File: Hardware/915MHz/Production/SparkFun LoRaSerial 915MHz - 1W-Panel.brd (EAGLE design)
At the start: 122.2 x 153.5 mm, 846 parts, among them J1 QWIIC_RIGHT_ANGLE, J11 USB C, J12 QWIIC_RIGHT_ANGLE, J13 JTAG, J16 USB C, J17 QWIIC_RIGHT_ANGLE, J18 JTAG, J2 USB C, J21 USB C, J22 QWIIC_RIGHT_ANGLE, J23 JTAG, J26 USB C, J27 QWIIC_RIGHT_ANGLE, J28 JTAG, J3 USB C, J31 USB C, J32 QWIIC_RIGHT_ANGLE, J33 JTAG, J36 USB C, J37 QWIIC_RIGHT_ANGLE, J38 JTAG, J4 JTAG, J41 USB C, J42 QWIIC_RIGHT_ANGLE, J43 JTAG, J46 USB C, J47 QWIIC_RIGHT_ANGLE, J48 JTAG, J7 QWIIC_RIGHT_ANGLE, J8 JTAG, Q1 20V/0.2A/8MHz/1.2Ω/1Vth, Q10 20V/0.2A/8MHz/1.2Ω/1Vth, Q11 20V/0.2A/8MHz/1.2Ω/1Vth, Q12 20V/0.2A/8MHz/1.2Ω/1Vth, Q13 20V/0.2A/8MHz/1.2Ω/1Vth, Q14 20V/0.2A/8MHz/1.2Ω/1Vth, Q15 20V/0.2A/8MHz/1.2Ω/1Vth, Q16 20V/0.2A/8MHz/1.2Ω/1Vth, Q17 20V/0.2A/8MHz/1.2Ω/1Vth, Q18 20V/0.2A/8MHz/1.2Ω/1Vth, Q19 20V/0.2A/8MHz/1.2Ω/1Vth, Q2 20V/0.2A/8MHz/1.2Ω/1Vth, Q20 20V/0.2A/8MHz/1.2Ω/1Vth, Q3 20V/0.2A/8MHz/1.2Ω/1Vth, Q4 20V/0.2A/8MHz/1.2Ω/1Vth, Q5 20V/0.2A/8MHz/1.2Ω/1Vth, Q6 20V/0.2A/8MHz/1.2Ω/1Vth, Q7 20V/0.2A/8MHz/1.2Ω/1Vth, Q8 20V/0.2A/8MHz/1.2Ω/1Vth, Q9 20V/0.2A/8MHz/1.2Ω/1Vth, U1 AP2112K-3.3, U10 AP2112K-3.3, U11 E19-915M30S, U12 ATSAMD21G-A, U13 AP2112K-3.3, U14 E19-915M30S, U15 ATSAMD21G-A, U16 AP2112K-3.3, U17 E19-915M30S, U18 ATSAMD21G-A, U19 AP2112K-3.3, U2 ATSAMD21G-A, U20 E19-915M30S, U21 ATSAMD21G-A, U22 AP2112K-3.3, U23 E19-915M30S, U24 ATSAMD21G-A, U25 AP2112K-3.3, U26 E19-915M30S, U27 ATSAMD21G-A, U28 AP2112K-3.3, U29 E19-915M30S, U3 AP2112K-3.3, U30 ATSAMD21G-A, U4 E19-915M30S, U5 E19-915M30S, U6 ATSAMD21G-A, U7 AP2112K-3.3, U8 E19-915M30S, U9 ATSAMD21G-A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

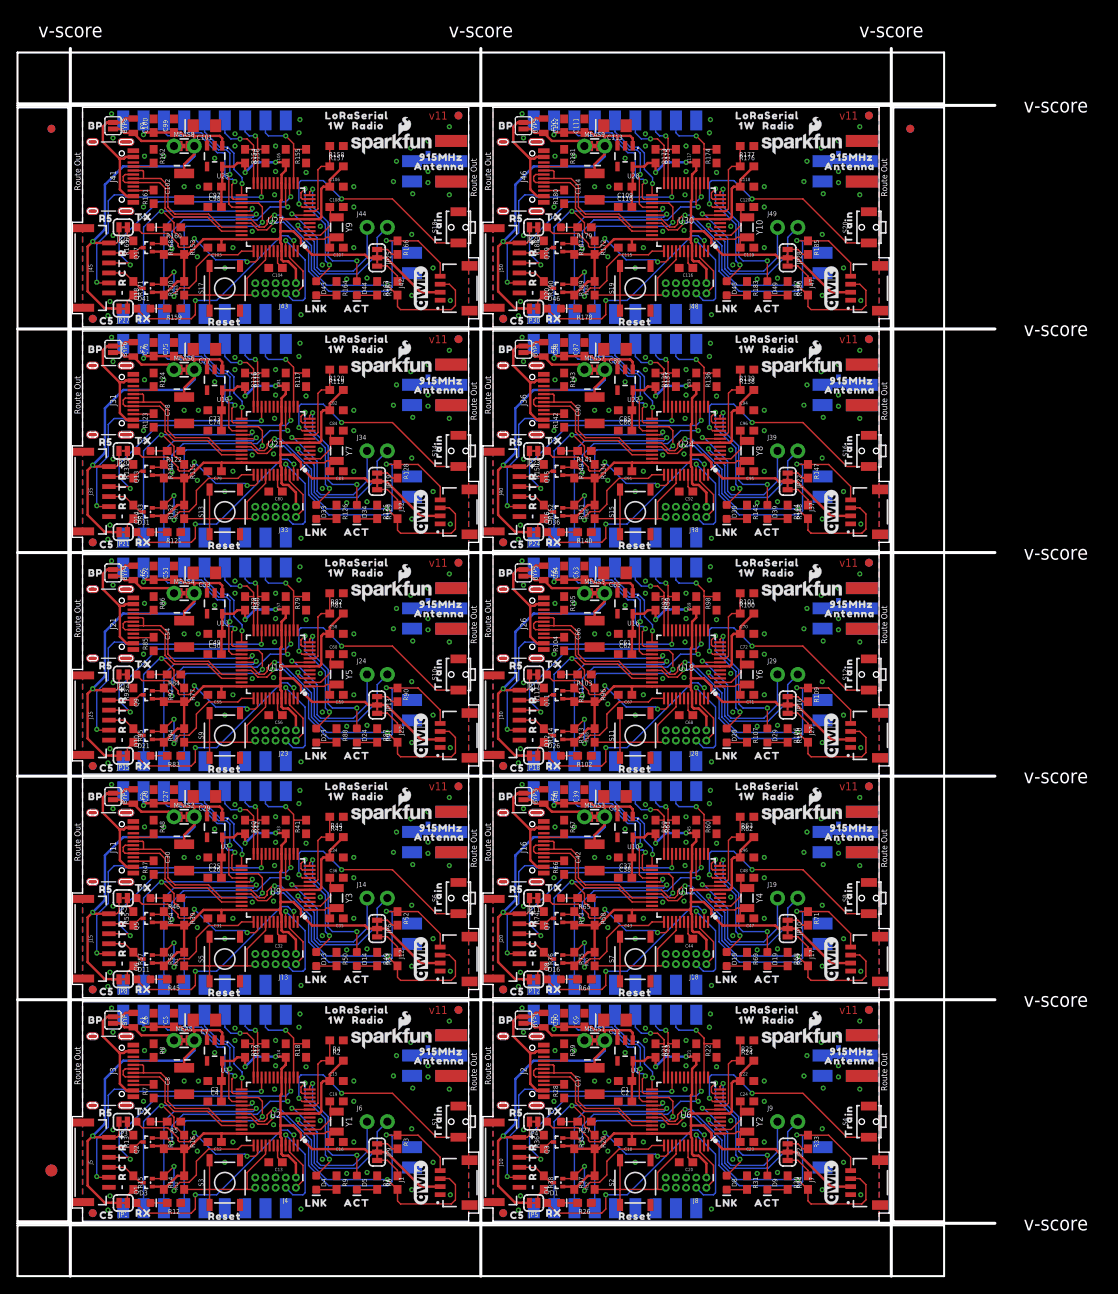
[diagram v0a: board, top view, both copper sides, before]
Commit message: Add RSSI LEDs
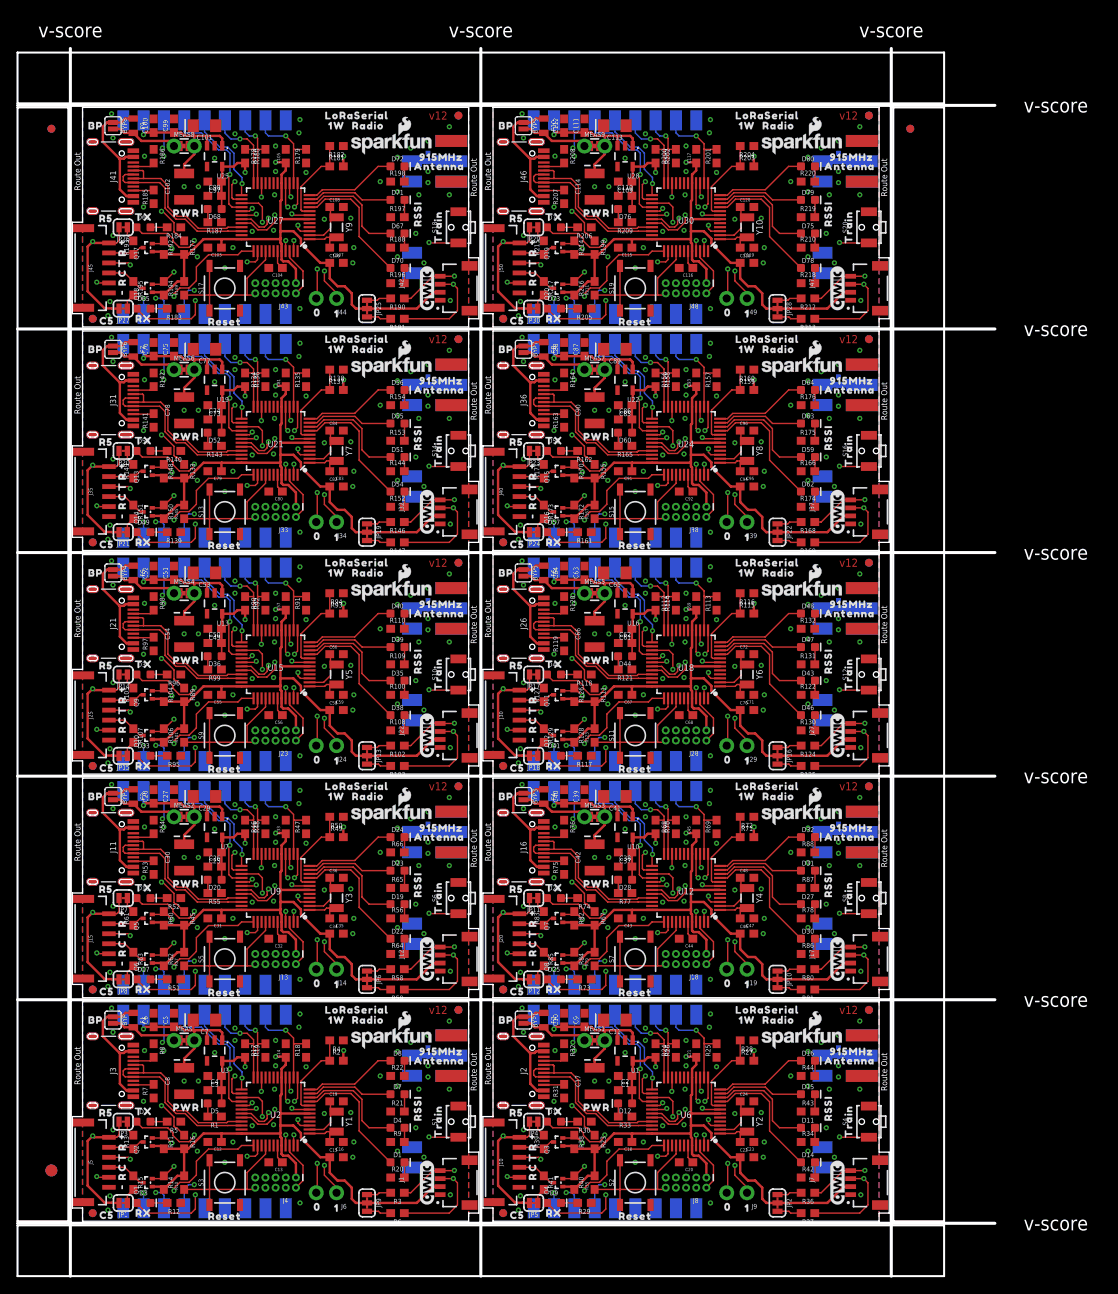
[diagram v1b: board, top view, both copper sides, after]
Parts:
- added D51, D54, D55, D56, D59, D62, D63, D64, D67, D70, D71, D72, D75, D78, D79, D80: GREEN, SparkFun-LED:LED-0603
- added D52, D60, D68, D76: RED, SparkFun-LED:LED-0603
- added D53, D61, D69, D77: PESD0402, SparkFun-DiscreteSemi:0402-TIGHT
- added D57, D65, D73: Yellow, SparkFun-LED:LED-0603
- added D58, D66, D74: BLUE, SparkFun-LED:LED-0603
- added R191, R192, R193, R194, R195, R212, R213, R214, R215, R216, R217: 2.2k, SparkFun-Resistors:0603
- added R196, R197, R198, R205, R210, R218, R219, R220: 4.7k, SparkFun-Resistors:0603
- added R199, R200, R201, R202: 100k, SparkFun-Resistors:0603
- added R203, R204, R211: 10k, SparkFun-Resistors:0603
- added R206, R209: 1k, SparkFun-Resistors:0603
- added R207, R208: 5.1k, SparkFun-Resistors:0603
- added U$201: (no value), output:ANTENNA1
- added U$202: (no value), output:RADIO2
- added U$203: (no value), output:RX1
- added U$204: (no value), output:TX0
- added U$205: (no value), output:#0
- added U$206: (no value), output:#1
- added U$207: (no value), output:R3
- added U$208: (no value), output:T2
- added U$209: (no value), output:C0
- added U$210: (no value), output:R1
- added U$211: (no value), output:LORASERIAL0
- added U$212: (no value), output:1W1
- added U$213: (no value), output:TRAIN0
- added U$214: (no value), output:BP0
- added U$215: (no value), output:C50
- added U$216: (no value), output:R50
- added U$217: (no value), output:RSSI0
- added U$218: (no value), output:PWR0
- added U$219: (no value), output:01
- added U$220: (no value), output:10
- D1, D11, D16, D31, D46: value Yellow -> GREEN
- D10, D50: value PESD0402 -> BLUE; device SparkFun-DiscreteSemi:0402-TIGHT -> SparkFun-LED:LED-0603
- D12: value GREEN -> RED
- D13: value BLUE -> PESD0402; device SparkFun-LED:LED-0603 -> SparkFun-DiscreteSemi:0402-TIGHT
- D14, D19, D24, D39: value RED -> GREEN
- D15, D30, D35, D40: value PESD0402 -> GREEN; device SparkFun-DiscreteSemi:0402-TIGHT -> SparkFun-LED:LED-0603
- D17: value GREEN -> Yellow
- D2, D42: value GREEN -> BLUE
- D20: value PESD0402 -> RED; device SparkFun-DiscreteSemi:0402-TIGHT -> SparkFun-LED:LED-0603
- D21: value Yellow -> PESD0402; device SparkFun-LED:LED-0603 -> SparkFun-DiscreteSemi:0402-TIGHT
- D23, D38, D4, D43, D48, D8: value BLUE -> GREEN
- D25: value PESD0402 -> Yellow; device SparkFun-DiscreteSemi:0402-TIGHT -> SparkFun-LED:LED-0603
- D26: value Yellow -> BLUE
- D28: value BLUE -> RED
- D29: value RED -> PESD0402; device SparkFun-LED:LED-0603 -> SparkFun-DiscreteSemi:0402-TIGHT
- D33: value BLUE -> Yellow
- D34: value RED -> BLUE
- D36: value Yellow -> RED
- D37: value GREEN -> PESD0402; device SparkFun-LED:LED-0603 -> SparkFun-DiscreteSemi:0402-TIGHT
- D49, D9: value RED -> Yellow
- R100, R108, R139, R176, R43, R44, R51: value 10k -> 4.7k
- R102, R103, R83, R84: value 4.7k -> 2.2k
- R104, R105, R124, R85: value 5.1k -> 2.2k
- R106, R107, R125, R126: value 1k -> 2.2k
- R109, R110, R130, R131, R132, R152, R166, R188, R34, R56, R73, R95: value 2.2k -> 4.7k
- R111, R112, R113, R114, R133, R90, R91, R92: value 2.2k -> 100k
- R115, R116, R137, R79: value 100k -> 10k
- R117, R153, R154, R174, R175, R20, R21, R22, R42, R78: value 100k -> 4.7k
- R118, R77, R96, R99: value 100k -> 1k
- R119, R120, R32: value 10k -> 5.1k
- R121, R140, R5: value 4.7k -> 1k
- R123, R181, R28: value 5.1k -> 10k
- R127, R146, R62, R63, R81, R82: value 10k -> 2.2k
- R141: value 4.7k -> 5.1k
- R143, R162: value 5.1k -> 1k
- R144, R183, R87, R88, R9: value 1k -> 4.7k
- R145, R182, R49, R50: value 1k -> 10k
- R157, R158, R177, R24, R25, R70, R89: value 10k -> 100k
- R159, R160, R27: value 4.7k -> 10k
- R161, R29, R66, R86: value 5.1k -> 4.7k
- R163, R164, R31: value 1k -> 5.1k
- R165, R184: value 10k -> 1k
- R167, R189, R35, R57, R71, R72, R93, R94: value 2.2k -> 10k
- R172, R173, R39, R40, R41, R58, R59, R60, R61, R80: value 100k -> 2.2k
- R178, R179, R26, R45, R46: value 4.7k -> 100k
- R180, R47, R48, R67: value 5.1k -> 100k
- R185, R186, R53, R54, R75, R76: value 2.2k -> 5.1k
- R187, R33, R52, R55, R74: value 2.2k -> 1k
- R68, R69: value 1k -> 100k
- R97, R98: value 100k -> 5.1k
- U$100: device output:R50 -> output:R1
- U$101: device output:RESET0 -> output:LORASERIAL0
- U$102: device output:915MHZ0 -> output:1W1
- U$103: device output:ANTENNA1 -> output:TRAIN0
- U$104: device output:RADIO2 -> output:BP0
- U$105: device output:ACT3 -> output:C50
- U$106: device output:LNK2 -> output:R50
- U$107: device output:RX1 -> output:RSSI0
- U$108: device output:TX0 -> output:PWR0
- U$109: device output:#0 -> output:01
- U$110: device output:#1 -> output:10
- U$111: device output:R3 -> output:RESET0
- U$112: device output:T2 -> output:915MHZ0
- U$113: device output:C0 -> output:ANTENNA1
- U$114: device output:R1 -> output:RADIO2
- U$115: device output:LORASERIAL0 -> output:RX1
- U$116: device output:1W1 -> output:TX0
- U$117: device output:TRAIN0 -> output:#0
- U$118: device output:BP0 -> output:#1
- U$119: device output:C50 -> output:R3
- U$120: device output:R50 -> output:T2
- U$121: device output:RESET0 -> output:C0
- U$122: device output:915MHZ0 -> output:R1
- U$123: device output:ANTENNA1 -> output:LORASERIAL0
- U$124: device output:RADIO2 -> output:1W1
- U$125: device output:ACT3 -> output:TRAIN0
- U$126: device output:LNK2 -> output:BP0
- U$127: device output:RX1 -> output:C50
- U$128: device output:TX0 -> output:R50
- U$129: device output:#0 -> output:RSSI0
- U$130: device output:#1 -> output:PWR0
- U$131: device output:R3 -> output:01
- U$132: device output:T2 -> output:10
- U$133: device output:C0 -> output:RESET0
- U$134: device output:R1 -> output:915MHZ0
- U$135: device output:LORASERIAL0 -> output:ANTENNA1
- U$136: device output:1W1 -> output:RADIO2
- U$137: device output:TRAIN0 -> output:RX1
- U$138: device output:BP0 -> output:TX0
- U$139: device output:C50 -> output:#0
- U$140: device output:R50 -> output:#1
- U$141: device output:RESET0 -> output:R3
- U$142: device output:915MHZ0 -> output:T2
- U$143: device output:ANTENNA1 -> output:C0
- U$144: device output:RADIO2 -> output:R1
- U$145: device output:ACT3 -> output:LORASERIAL0
- U$146: device output:LNK2 -> output:1W1
- U$147: device output:RX1 -> output:TRAIN0
- U$148: device output:TX0 -> output:BP0
- U$149: device output:#0 -> output:C50
- U$150: device output:#1 -> output:R50
- U$151: device output:R3 -> output:RSSI0
- U$152: device output:T2 -> output:PWR0
- U$153: device output:C0 -> output:01
- U$154: device output:R1 -> output:10
- U$155: device output:LORASERIAL0 -> output:RESET0
- U$156: device output:1W1 -> output:915MHZ0
- U$157: device output:TRAIN0 -> output:ANTENNA1
- U$158: device output:BP0 -> output:RADIO2
- U$159: device output:C50 -> output:RX1
- U$160: device output:R50 -> output:TX0
- U$161: device output:RESET0 -> output:#0
- U$162: device output:915MHZ0 -> output:#1
- U$163: device output:ANTENNA1 -> output:R3
- U$164: device output:RADIO2 -> output:T2
- U$165: device output:ACT3 -> output:C0
- U$166: device output:LNK2 -> output:R1
- U$167: device output:RX1 -> output:LORASERIAL0
- U$168: device output:TX0 -> output:1W1
- U$169: device output:#0 -> output:TRAIN0
- U$170: device output:#1 -> output:BP0
- U$171: device output:R3 -> output:C50
- U$172: device output:T2 -> output:R50
- U$173: device output:C0 -> output:RSSI0
- U$174: device output:R1 -> output:PWR0
- U$175: device output:LORASERIAL0 -> output:01
- U$176: device output:1W1 -> output:10
- U$177: device output:TRAIN0 -> output:RESET0
- U$178: device output:BP0 -> output:915MHZ0
- U$179: device output:C50 -> output:ANTENNA1
- U$180: device output:R50 -> output:RADIO2
- U$181: device output:RESET0 -> output:RX1
- U$182: device output:915MHZ0 -> output:TX0
- U$183: device output:ANTENNA1 -> output:#0
- U$184: device output:RADIO2 -> output:#1
- U$185: device output:ACT3 -> output:R3
- U$186: device output:LNK2 -> output:T2
- U$187: device output:RX1 -> output:C0
- U$188: device output:TX0 -> output:R1
- U$189: device output:#0 -> output:LORASERIAL0
- U$190: device output:#1 -> output:1W1
- U$191: device output:R3 -> output:TRAIN0
- U$192: device output:T2 -> output:BP0
- U$193: device output:C0 -> output:C50
- U$194: device output:R1 -> output:R50
- U$195: device output:LORASERIAL0 -> output:RSSI0
- U$196: device output:1W1 -> output:PWR0
- U$197: device output:TRAIN0 -> output:01
- U$198: device output:BP0 -> output:10
- U$199: device output:C50 -> output:RESET0
- U$200: device output:R50 -> output:915MHZ0
- U$21, U$41: device output:RESET0 -> output:RSSI0
- U$22: device output:915MHZ0 -> output:10
- U$23: device output:ANTENNA1 -> output:RESET0
- U$24: device output:RADIO2 -> output:915MHZ0
- U$25: device output:ACT3 -> output:ANTENNA1
- U$26: device output:LNK2 -> output:RADIO2
- U$42: device output:915MHZ0 -> output:PWR0
- U$43: device output:ANTENNA1 -> output:01
- U$44: device output:RADIO2 -> output:10
- U$45: device output:ACT3 -> output:RESET0
- U$46: device output:LNK2 -> output:915MHZ0
- U$47: device output:RX1 -> output:ANTENNA1
- U$48: device output:TX0 -> output:RADIO2
- U$49: device output:#0 -> output:RX1
- U$50: device output:#1 -> output:TX0
- U$51: device output:R3 -> output:#0
- U$52: device output:T2 -> output:#1
- U$53: device output:C0 -> output:R3
- U$54: device output:R1 -> output:T2
- U$55: device output:LORASERIAL0 -> output:C0
- U$56: device output:1W1 -> output:R1
- U$57: device output:TRAIN0 -> output:LORASERIAL0
- U$58: device output:BP0 -> output:1W1
- U$59: device output:C50 -> output:TRAIN0
- U$6, U$65: device output:ACT3 -> output:01
- U$60: device output:R50 -> output:BP0
- U$61: device output:RESET0 -> output:C50
- U$62: device output:915MHZ0 -> output:R50
- U$63: device output:ANTENNA1 -> output:RSSI0
- U$64: device output:RADIO2 -> output:PWR0
- U$66: device output:LNK2 -> output:10
- U$67: device output:RX1 -> output:RESET0
- U$68: device output:TX0 -> output:915MHZ0
- U$69: device output:#0 -> output:ANTENNA1
- U$7, U$86: device output:LNK2 -> output:PWR0
- U$70: device output:#1 -> output:RADIO2
- U$71: device output:R3 -> output:RX1
- U$72: device output:T2 -> output:TX0
- U$73: device output:C0 -> output:#0
- U$74: device output:R1 -> output:#1
- U$75: device output:LORASERIAL0 -> output:R3
- U$76: device output:1W1 -> output:T2
- U$77: device output:TRAIN0 -> output:C0
- U$78: device output:BP0 -> output:R1
- U$79: device output:C50 -> output:LORASERIAL0
- U$80: device output:R50 -> output:1W1
- U$81: device output:RESET0 -> output:TRAIN0
- U$82: device output:915MHZ0 -> output:BP0
- U$83: device output:ANTENNA1 -> output:C50
- U$84: device output:RADIO2 -> output:R50
- U$85: device output:ACT3 -> output:RSSI0
- U$87: device output:RX1 -> output:01
- U$88: device output:TX0 -> output:10
- U$89: device output:#0 -> output:RESET0
- U$90: device output:#1 -> output:915MHZ0
- U$91: device output:R3 -> output:ANTENNA1
- U$92: device output:T2 -> output:RADIO2
- U$93: device output:C0 -> output:RX1
- U$94: device output:R1 -> output:TX0
- U$95: device output:LORASERIAL0 -> output:#0
- U$96: device output:1W1 -> output:#1
- U$97: device output:TRAIN0 -> output:R3
- U$98: device output:BP0 -> output:T2
- U$99: device output:C50 -> output:C0
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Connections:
- removed net A20: U21.10
- removed net A21: J39.1, U24.7
- removed net A22: J39.2, U24.3
- removed net A23: U24.10
- removed net A24: J44.1, U27.7
- removed net A25: J44.2, U27.3
- removed net A26: U27.10
- removed net A27: J49.1, U30.7
- removed net A28: J49.2, U30.3
- removed net A29: U30.10
- removed net A3/TRAIN: S1.1, U2.9
- removed net A3/TRAIN1: S4.1, U6.9
- removed net A3/TRAIN2: S6.1, U9.9
- removed net A3/TRAIN3: S8.1, U12.9
- removed net A3/TRAIN4: S10.1, U15.9
- removed net A3/TRAIN5: S12.1, U18.9
- removed net A3/TRAIN6: S14.1, U21.9
- removed net A3/TRAIN7: S16.1, U24.9
- removed net A3/TRAIN8: S18.1, U27.9
- removed net A3/TRAIN9: S20.1, U30.9
- removed net D31: U24.19
- removed net D32: U24.20
- removed net D33: U27.13
- removed net D34: U27.21
- removed net D35: U27.19
- removed net D36: U27.20
- removed net D37: U30.13
- removed net D38: U30.21
- removed net D39: U30.19
- removed net D40: U30.20
- removed net D8/LINK: D4.A, U2.11
- removed net D8/LINK1: D8.A, U6.11
- removed net D8/LINK2: D13.A, U9.11
- removed net D8/LINK3: D18.A, U12.11
- removed net D8/LINK4: D23.A, U15.11
- removed net D8/LINK5: D28.A, U18.11
- removed net D8/LINK6: D33.A, U21.11
- removed net D8/LINK7: D38.A, U24.11
- removed net D8/LINK8: D43.A, U27.11
- removed net D8/LINK9: D48.A, U30.11
- removed net D9/ACT: D5.A, U2.12
- removed net D9/ACT1: D9.A, U6.12
- removed net D9/ACT2: D14.A, U9.12
- removed net D9/ACT3: D19.A, U12.12
- removed net D9/ACT4: D24.A, U15.12
- removed net D9/ACT5: D29.A, U18.12
- removed net D9/ACT6: D34.A, U21.12
- removed net D9/ACT7: D39.A, U24.12
- removed net D9/ACT8: D44.A, U27.12
- removed net D9/ACT9: D49.A, U30.12
- removed net N$14 (its old number): D7.C, R27.2
- removed net N$15 (its old number): JP4.1, R36.2
- removed net N$25 (its old number): D19.C, R68.2
- removed net N$26 (its old number): D18.C, R69.2
- removed net N$37 (its old number): D21.C, R83.2
- removed net N$47 (its old number): JP17.1, R112.2
- removed net N$48 (its old number): JP18.1, R114.2
- removed net N$58 (its old number): D38.C, R145.2
- removed net N$69 (its old number): D41.C, R159.2
- removed net N$70 (its old number): D42.C, R160.2
- removed net N$80 (its old number): JP30.1, R190.2
- new net A3/RSSI1: D1.A, U2.9
- new net A3/RSSI10: D78.A, U30.9
- new net A3/RSSI2: D14.A, U6.9
- new net A3/RSSI3: D22.A, U9.9
- new net A3/RSSI4: D30.A, U12.9
- new net A3/RSSI5: D38.A, U15.9
- new net A3/RSSI6: D46.A, U18.9
- new net A3/RSSI7: D54.A, U21.9
- new net A3/RSSI8: D62.A, U24.9
- new net A3/RSSI9: D70.A, U27.9
- new net A4/RSSI1: D11.A, U6.10
- new net A4/RSSI10: D75.A, U30.10
- new net A4/RSSI2: D4.A, U2.10
- new net A4/RSSI3: D19.A, U9.10
- new net A4/RSSI4: D27.A, U12.10
- new net A4/RSSI5: D35.A, U15.10
- new net A4/RSSI6: D43.A, U18.10
- new net A4/RSSI7: D51.A, U21.10
- new net A4/RSSI8: D59.A, U24.10
- new net A4/RSSI9: D67.A, U27.10
- new net D4/TRAIN: S1.1, U2.13
- new net D4/TRAIN1: S4.1, U6.13
- new net D4/TRAIN2: S6.1, U9.13
- new net D4/TRAIN3: S8.1, U12.13
- new net D4/TRAIN4: S10.1, U15.13
- new net D4/TRAIN5: S12.1, U18.13
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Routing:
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- added copper zone on layer 15, net GND
- added copper zone on layer 2, net GND
- added copper zone on layer 15, net GND1
- added copper zone on layer 2, net GND1
- added copper zone on layer 15, net GND2
- added copper zone on layer 2, net GND2
- added copper zone on layer 15, net GND3
- added copper zone on layer 2, net GND3
- added copper zone on layer 15, net GND4
- added copper zone on layer 2, net GND4
- added copper zone on layer 15, net GND5
- added copper zone on layer 2, net GND5
- added copper zone on layer 15, net GND6
- added copper zone on layer 2, net GND6
- added copper zone on layer 15, net GND7
- added copper zone on layer 2, net GND7
- added copper zone on layer 15, net GND8
- added copper zone on layer 2, net GND8
- added copper zone on layer 15, net GND9
- added copper zone on layer 2, net GND9
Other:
- board text added: "v12"
- board text removed: "v11"

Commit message: Adjust 50ohm microstrip for four layer
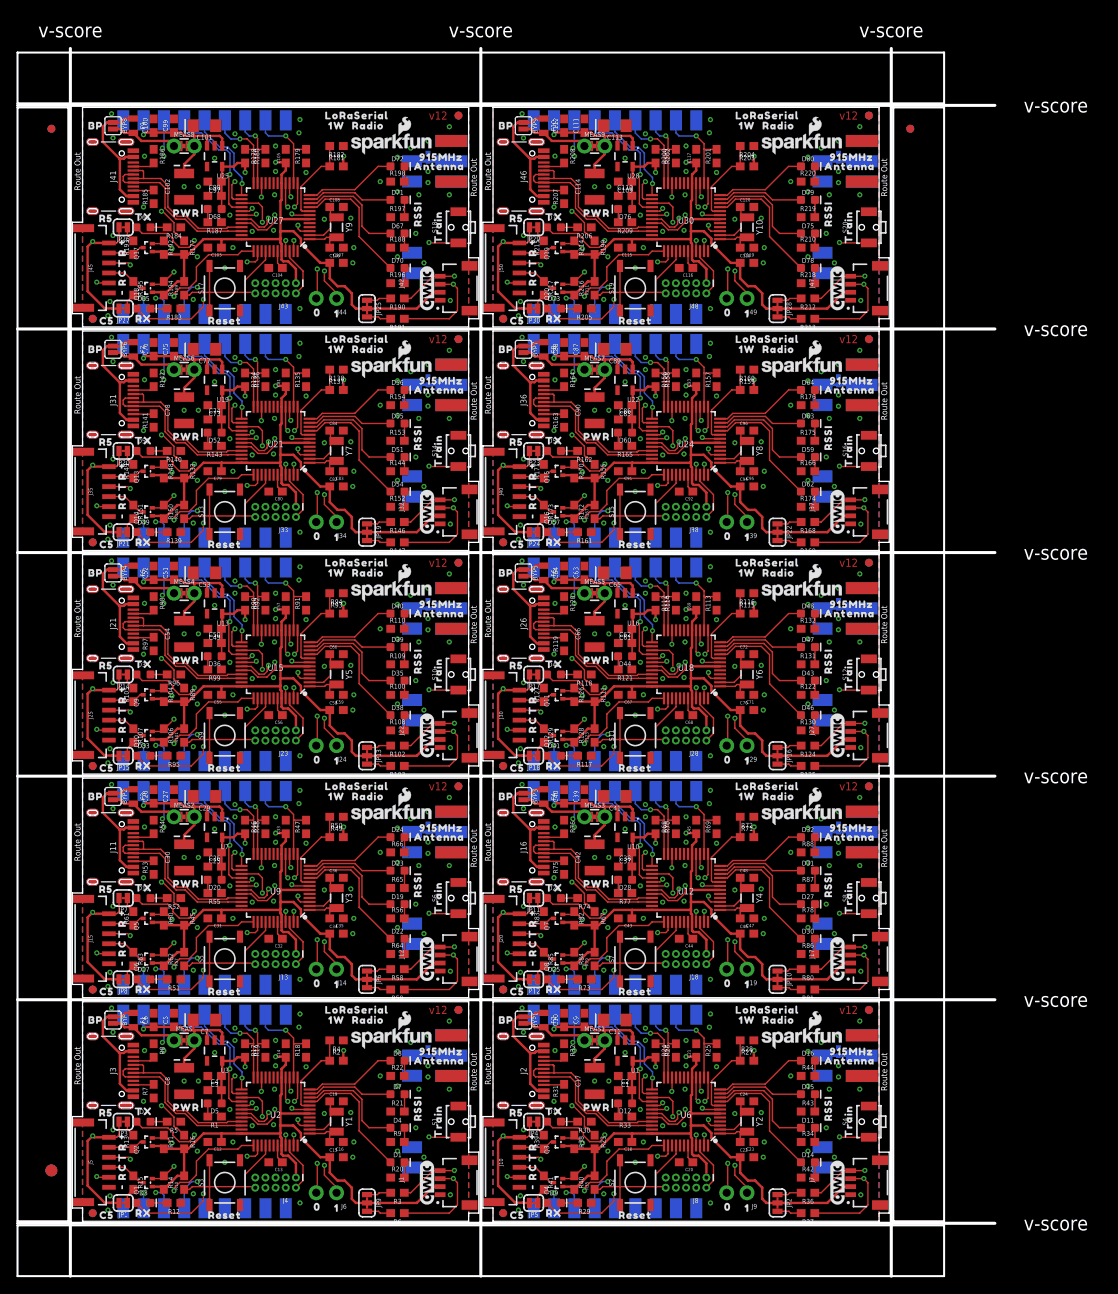
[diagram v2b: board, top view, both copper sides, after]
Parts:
- moved U$177 0.13 mm to (19.1, 112.6)
- moved U$199 0.13 mm to (70.4, 112.6)
- moved U$111 0.13 mm to (70.4, 56.7)
- moved U$89 0.13 mm to (19.1, 56.7)
- moved U$2 0.13 mm to (19.1, 0.77)
- moved U$23 0.13 mm to (70.4, 0.77)
- moved U$45 0.13 mm to (19.1, 28.7)
- moved U$67 0.13 mm to (70.4, 28.7)
- moved U$133 0.13 mm to (19.1, 84.6)
- moved U$155 0.13 mm to (70.4, 84.6)
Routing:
- net D10/LORA_D9: track 25.8 -> 26.6 mm
- net D10/LORA_D8: track 25.8 -> 26.6 mm
- net D10/LORA_D7: track 25.8 -> 26.6 mm
- net D10/LORA_D6: track 25.8 -> 26.6 mm
- net D10/LORA_D5: track 25.8 -> 26.6 mm
- net D10/LORA_D3: track 25.8 -> 26.6 mm
- net D10/LORA_D2: track 25.8 -> 26.6 mm
- net D10/LORA_D1: track 25.8 -> 26.6 mm
- net D10/LORA_D4: track 25.8 -> 26.6 mm
- net D10/LORA_D10: track 25.8 -> 26.6 mm
- net A5/RX_LED9: track 27.1 -> 26.6 mm
- net A5/RX_LED7: track 27.1 -> 26.6 mm
- net A5/RX_LED5: track 27.1 -> 26.6 mm
- net A5/RX_LED3: track 27.1 -> 26.6 mm
- net A5/RX_LED1: track 27.1 -> 26.6 mm
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
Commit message: v13 - panel files.
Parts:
- removed BYP, BYP1, BYP2, BYP3, BYP4, BYP5, BYP6, BYP7, BYP8, BYP9: JUMPER-SMT_2_NO_SILK, SparkFun-Jumpers:SMT-JUMPER_2_NO_SILK
- removed C111: 0.22uF, SparkFun-Capacitors:0603
- removed C112, C115, C116, C117, C118: 0.1uF, SparkFun-Capacitors:0603
- removed C113: 10uF, SparkFun-Capacitors:EIA3216
- removed C114: 47uF, SparkFun-Capacitors:EIA3528
- removed C119, C120: 15pF, SparkFun-Capacitors:0603
- removed MEAS, MEAS1, MEAS2, MEAS3, MEAS4, MEAS5, MEAS6, MEAS7, MEAS8, MEAS9: JUMPER-COMBO_2_NC_TRACE, SparkFun-Jumpers:COMBO-JUMPER_2_NC_TRACE
- added D81, D90: 3A/10V/280mV, SparkFun-DiscreteSemi:SOD-323
- added D82: Yellow, SparkFun-LED:LED-0603
- added D83: BLUE, SparkFun-LED:LED-0603
- added D84, D87, D88, D89: GREEN, SparkFun-LED:LED-0603
- added D85: RED, SparkFun-LED:LED-0603
- added D86: PESD0402, SparkFun-DiscreteSemi:0402-TIGHT
- added JP31, JP34, JP35, JP38, JP39: JUMPER-SMT_2_NC_TRACE_SILK, SparkFun-Jumpers:SMT-JUMPER_2_NC_TRACE_SILK
- added JP32, JP36, JP40: (no value), SparkFun-Jumpers:SMT-JUMPER_2_NC_TRACE_SILK
- added JP33, JP37: JUMPER-SMT_3_2-NC_TRACE_SILK, SparkFun-Jumpers:SMT-JUMPER_3_2-NC_TRACE_SILK
- added Q21, Q22, Q27, Q28, Q29, Q30, Q35, Q36, Q37, Q38, Q43, Q44, Q45, Q46, Q51, Q52, Q53, Q54, Q59, Q60, Q61, Q62, Q67, Q68, Q69, Q70, Q75, Q76, Q77, Q78: 600mA/40V, SparkFun-DiscreteSemi:SOT23-3
- added Q23, Q31, Q39, Q47, Q55, Q63, Q71, Q79: (no value), SparkFun-DiscreteSemi:SOT363_PHILIPS
- added Q24, Q32, Q40, Q48, Q56, Q64, Q72, Q80: 20V/4.2A/52mΩ/1.4W, SparkFun-DiscreteSemi:SOT23-3
- added Q25, Q26, Q33, Q34, Q41, Q42, Q49, Q50, Q57, Q58, Q65, Q66, Q73, Q74: 20V/0.2A/8MHz/1.2Ω/1Vth, SparkFun-DiscreteSemi:SOT-416FL
- added R221, R222, R235, R247, R248, R249, R250, R263, R275, R276, R277, R278: 1k, SparkFun-Resistors:0603
- added R223, R225, R226, R227, R228, R251, R253, R254, R255, R256, R279: 100k, SparkFun-Resistors:0603
- added R224, R252, R280: 1M, SparkFun-Resistors:0603
- added R229, R230, R237, R257, R258, R265: 10k, SparkFun-Resistors:0603
- added R231, R259: 330, SparkFun-Resistors:0603
- added R232, R260: 0, SparkFun-Resistors:0603
- added R233, R234, R261, R262: 5.1k, SparkFun-Resistors:0603
- added R236, R244, R245, R246, R264, R272, R273, R274: 220, SparkFun-Resistors:0603
- added R238, R239, R240, R241, R242, R243, R266, R267, R268, R269, R270, R271: 2.2k, SparkFun-Resistors:0603
- added TP1, TP10, TP100, TP101, TP102, TP103, TP104, TP105, TP106, TP107, TP108, TP109, TP11, TP110, TP111, TP112, TP113, TP114, TP115, TP116, TP117, TP118, TP119, TP12, TP120, TP121, TP122, TP123, TP124, TP125, TP126, TP127, TP128, TP129, TP13, TP130, TP14, TP15, TP16, TP17, TP18, TP19, TP2, TP20, TP21, TP22, TP23, TP24, TP25, TP26, TP27, TP28, TP29, TP3, TP30, TP31, TP32, TP33, TP34, TP35, TP36, TP37, TP38, TP39, TP4, TP40, TP41, TP42, TP43, TP44, TP45, TP46, TP47, TP48, TP49, TP5, TP50, TP51, TP52, TP53, TP54, TP55, TP56, TP57, TP58, TP59, TP6, TP60, TP61, TP62, TP63, TP64, TP65, TP66, TP67, TP68, TP69, TP7, TP70, TP71, TP72, TP73, TP74, TP75, TP76, TP77, TP78, TP79, TP8, TP80, TP81, TP82, TP83, TP84, TP85, TP86, TP87, TP88, TP89, TP9, TP90, TP91, TP92, TP93, TP94, TP95, TP96, TP97, TP98, TP99: (no value), SparkFun-Connectors:PAD.03X.05
- C10, C104, C38, C82, C93: value 0.1uF -> 47uF; device SparkFun-Capacitors:0603 -> SparkFun-Capacitors:EIA3528
- C100, C34, C45, C56, C58, C6, C67, C69, C80, C91: value 0.1uF -> 1.0uF
- C101, C11, C29, C41, C53: value 10uF -> 0.1uF; device SparkFun-Capacitors:EIA3216 -> SparkFun-Capacitors:0603
- C102, C78: value 47uF -> 1.0uF; device SparkFun-Capacitors:EIA3528 -> SparkFun-Capacitors:0603
- C103, C26, C70, C81, C92: value 0.1uF -> 10uF; device SparkFun-Capacitors:0603 -> SparkFun-Capacitors:EIA3216
- C107, C108, C24, C35, C72, C83, C84, C95, C96: value 15pF -> 0.1uF
- C109: value 1.0uF -> 15pF
- C110, C21, C22, C32, C33, C43, C44, C55, C76, C88, C98: value 0.1uF -> 15pF
- C17, C30, C42, C90: value 47uF -> 0.1uF; device SparkFun-Capacitors:EIA3528 -> SparkFun-Capacitors:0603
- C23, C36, C47: value 15pF -> 1.0uF
- C27: value 0.22uF -> 47uF; device SparkFun-Capacitors:0603 -> SparkFun-Capacitors:EIA3528
- C37: value 1.0uF -> 10uF; device SparkFun-Capacitors:0603 -> SparkFun-Capacitors:EIA3216
- C39, C51, C63, C75: value 0.22uF -> 0.1uF
- C48, C59: value 15pF -> 10uF; device SparkFun-Capacitors:0603 -> SparkFun-Capacitors:EIA3216
- C49: value 1.0uF -> 47uF; device SparkFun-Capacitors:0603 -> SparkFun-Capacitors:EIA3528
- C5: value 0.22uF -> 1.0uF
- C54, C66: value 47uF -> 15pF; device SparkFun-Capacitors:EIA3528 -> SparkFun-Capacitors:0603
- C60, C71: value 15pF -> 47uF; device SparkFun-Capacitors:0603 -> SparkFun-Capacitors:EIA3528
- C61, C73, C85, C97: value 1.0uF -> 0.1uF
- C65, C77: value 10uF -> 15pF; device SparkFun-Capacitors:EIA3216 -> SparkFun-Capacitors:0603
- C87, C99: value 0.22uF -> 15pF
- C89: value 10uF -> 1.0uF; device SparkFun-Capacitors:EIA3216 -> SparkFun-Capacitors:0603
- C9: value 0.22uF -> 10uF; device SparkFun-Capacitors:0603 -> SparkFun-Capacitors:EIA3216
- D10: value BLUE -> Yellow
- D11, D38, D47, D56: value GREEN -> BLUE
- D12, D44, D52, D60: value RED -> GREEN
- D13: value PESD0402 -> RED; device SparkFun-DiscreteSemi:0402-TIGHT -> SparkFun-LED:LED-0603
- D14, D23, D32, D59: value GREEN -> PESD0402; device SparkFun-LED:LED-0603 -> SparkFun-DiscreteSemi:0402-TIGHT
- D17, D25, D33, D57: value Yellow -> GREEN
- D18: value BLUE -> 3A/10V/280mV; device SparkFun-LED:LED-0603 -> SparkFun-DiscreteSemi:SOD-323
- D19, D46, D55, D64: value GREEN -> Yellow
- D20: value RED -> BLUE
- D21, D53, D61, D69: value PESD0402 -> GREEN; device SparkFun-DiscreteSemi:0402-TIGHT -> SparkFun-LED:LED-0603
- D22, D31, D40, D67: value GREEN -> RED
- D26, D34, D42, D66: value BLUE -> GREEN
- D27, D54, D63, D72: value GREEN -> 3A/10V/280mV; device SparkFun-LED:LED-0603 -> SparkFun-DiscreteSemi:SOD-323
- D28: value RED -> Yellow
- D29: value PESD0402 -> BLUE; device SparkFun-DiscreteSemi:0402-TIGHT -> SparkFun-LED:LED-0603
- D36: value RED -> 3A/10V/280mV; device SparkFun-LED:LED-0603 -> SparkFun-DiscreteSemi:SOD-323
- D37: value PESD0402 -> Yellow; device SparkFun-DiscreteSemi:0402-TIGHT -> SparkFun-LED:LED-0603
- D41: value Yellow -> PESD0402; device SparkFun-LED:LED-0603 -> SparkFun-DiscreteSemi:0402-TIGHT
- D45: value PESD0402 -> 3A/10V/280mV; device SparkFun-DiscreteSemi:0402-TIGHT -> SparkFun-DiscreteSemi:SOD-323
- D49: value Yellow -> RED
- D50: value BLUE -> PESD0402; device SparkFun-LED:LED-0603 -> SparkFun-DiscreteSemi:0402-TIGHT
- D58: value BLUE -> RED
- D65: value Yellow -> BLUE
- D68: value RED -> PESD0402; device SparkFun-LED:LED-0603 -> SparkFun-DiscreteSemi:0402-TIGHT
- D9: value Yellow -> 3A/10V/280mV; device SparkFun-LED:LED-0603 -> SparkFun-DiscreteSemi:SOD-323
- JP10, JP19, JP22, JP6: value JUMPER-SMT_3_2-NC_TRACE_SILK -> JUMPER-SMT_2_NC_TRACE_SILK; device SparkFun-Jumpers:SMT-JUMPER_3_2-NC_TRACE_SILK -> SparkFun-Jumpers:SMT-JUMPER_2_NC_TRACE_SILK
- JP12, JP20, JP24, JP7: value JUMPER-SMT_2_NC_TRACE_SILK -> (none)
- JP16, JP2, JP28: value JUMPER-SMT_3_2-NC_TRACE_SILK -> (none); device SparkFun-Jumpers:SMT-JUMPER_3_2-NC_TRACE_SILK -> SparkFun-Jumpers:SMT-JUMPER_2_NC_TRACE_SILK
- JP17, JP21, JP29, JP4, JP8: value JUMPER-SMT_2_NC_TRACE_SILK -> JUMPER-SMT_3_2-NC_TRACE_SILK; device SparkFun-Jumpers:SMT-JUMPER_2_NC_TRACE_SILK -> SparkFun-Jumpers:SMT-JUMPER_3_2-NC_TRACE_SILK
- LOGO1, LOGO13, LOGO17, LOGO21, LOGO25, LOGO29, LOGO33, LOGO37, LOGO5, LOGO9: value SFE_LOGO_NAME_FLAME10_MM -> SFE_LOGO_NAME9_MM; device SparkFun-Aesthetics:SFE_LOGO_NAME_FLAME_10MM -> SparkFun-Aesthetics:SFE_LOGO_NAME_9MM
- LOGO10, LOGO14, LOGO18, LOGO2, LOGO22, LOGO26, LOGO30, LOGO34, LOGO38, LOGO6: value SFE_LOGO_NAME_FLAME.1_INCH -> SFE_LOGO_NAME_FLAME9_MM; device SparkFun-Aesthetics:SFE_LOGO_NAME_FLAME_.1 -> SparkFun-Aesthetics:SFE_LOGO_NAME_FLAME_9MM
- Q11, Q12, Q13, Q14, Q19, Q20, Q3, Q4, Q5, Q6: value 20V/0.2A/8MHz/1.2Ω/1Vth -> 600mA/40V; device SparkFun-DiscreteSemi:SOT-416FL -> SparkFun-DiscreteSemi:SOT23-3
- Q15, Q7: value 20V/0.2A/8MHz/1.2Ω/1Vth -> (none); device SparkFun-DiscreteSemi:SOT-416FL -> SparkFun-DiscreteSemi:SOT363_PHILIPS
- Q16, Q8: value 20V/0.2A/8MHz/1.2Ω/1Vth -> 20V/4.2A/52mΩ/1.4W; device SparkFun-DiscreteSemi:SOT-416FL -> SparkFun-DiscreteSemi:SOT23-3
- R100, R130, R131, R154, R183, R210, R42, R43, R44, R73: value 4.7k -> 2.2k
- R101, R159, R182, R211, R71, R72: value 10k -> 2.2k
- R104, R105, R106, R124, R190, R216, R217, R40: value 2.2k -> 220
- R107, R151, R191, R192, R193, R194, R39, R80, R81, R82: value 2.2k -> 1k
- R108, R109, R110, R166, R219, R220, R51, R95: value 4.7k -> 1k
- R112: value 100k -> 1M
- R115, R116, R167, R27, R57: value 10k -> 100k
- R117, R153, R174, R34: value 4.7k -> 10k
- R118, R209, R33: value 1k -> 10k
- R119: value 5.1k -> 330
- R12, R175: value 4.7k -> 330
- R120: value 5.1k -> 0
- R121, R206: value 1k -> 5.1k
- R122, R205, R65, R66: value 4.7k -> 5.1k
- R123, R137, R138, R79: value 10k -> 1k
- R125, R146, R173, R41, R61, R62: value 2.2k -> 10k
- R132, R152, R161, R188, R20, R21, R218, R22, R78, R9: value 4.7k -> 220
- R133, R134, R180, R48, R68: value 100k -> 220
- R135, R136, R179, R23, R24, R25, R26, R67: value 100k -> 1k
- R139, R144, R197, R198, R29, R86, R87, R88: value 4.7k -> 100k
- R140: value 1k -> 1M
- R141, R142, R31, R32: value 5.1k -> 100k
- R143, R30, R55: value 1k -> 100k
- R147, R63: value 2.2k -> 330
- R148, R36: value 2.2k -> 0
- R149, R150, R37, R38: value 2.2k -> 5.1k
- R155, R156, R157, R158, R45, R46, R47, R70: value 100k -> 2.2k
- R160, R189, R49, R50: value 10k -> 220
- R162, R77, R96: value 1k -> 220
- R163, R164, R207, R53, R54: value 5.1k -> 1k
- R168, R84: value 2.2k -> 1M
- R169, R170, R171, R172, R195, R58, R59, R60, R83, R85: value 2.2k -> 100k
- R176, R64: value 4.7k -> 0
- R177, R178: value 100k -> 5.1k
- R184, R187, R74, R99: value 1k -> 2.2k
- R185, R186, R75, R98: value 5.1k -> 2.2k
- R196, R56: value 4.7k -> 1M
- R201, R202, R69, R89, R90: value 100k -> 10k
- R203, R35: value 10k -> 330
- R204: value 10k -> 0
- R208, R76: value 5.1k -> 220
- R28: value 10k -> 1M
- R5: value 1k -> 0
- R91: value 100k -> 330
- R92: value 100k -> 0
- R93, R94: value 10k -> 5.1k
- R97: value 5.1k -> 10k
- U$104, U$126, U$148, U$170, U$192, U$214, U$38, U$60, U$82: device output:BP0 -> output:C50
- U$105, U$127, U$149, U$171, U$193, U$215, U$39, U$61, U$83: device output:C50 -> output:R50
- U$106, U$128, U$150, U$172, U$194, U$216, U$40, U$62, U$84: device output:R50 -> output:RSSI0
- U$107, U$129, U$151, U$173, U$195, U$217, U$41, U$63, U$85: device output:RSSI0 -> output:PWR0
- U$108, U$130, U$152, U$174, U$196, U$218, U$42, U$64, U$86: device output:PWR0 -> output:01
- U$109, U$131, U$153, U$175, U$197, U$219, U$43, U$65, U$87: device output:01 -> output:10
- U$110, U$132, U$154, U$176, U$198, U$220, U$44, U$66, U$88: device output:10 -> output:SH0
- U$23: device output:RESET0 -> output:SH0
- U$8: device output:BP0 -> output:RESET0
- U11, U14, U17, U20, U23, U26, U29, U4, U5, U8: device SparkFun-RF:E19-915MS1W -> SparkFun-RF:E19-915M30S
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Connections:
- removed net N$95 (its old number): JP26.1, R193.2
- new net N$111: D49.C, R151.2
- new net N$112: D48.C, R152.2
- new net N$113: C65.2, U18.1, Y6.P$2
- new net N$114: C66.1, U18.2, Y6.P$1
- new net N$115: D46.C, R147.2
- new net N$116: D47.C, R148.2
- new net N$117: JP22.1, R157.2
- new net N$118: JP23.1, R159.2
- new net N$119: D51.C, R160.2
- new net N$120: D52.C, R161.2
- new net N$121: D53.C, R162.2
- new net N$122: Q43.3, R160.1
- new net N$123: Q43.1, R163.1
- new net N$124: Q44.3, R152.1
- new net N$125: Q44.1, R164.1
- new net N$126: Q45.3, R161.1
- new net N$127: Q45.1, R165.1
- new net N$128: Q46.3, R162.1
- new net N$129: Q46.1, R166.1
- new net N$130: J26.SHLD1, J26.SHLD2, J26.SHLD3, J26.SHLD4, J26.SHLD5, J26.SHLD6, J26.SHLD7, J26.SHLD8, JP24.2
- new net N$131: Q47.3, Q48.1, R168.2
- new net N$132: Q47.2, Q47.5, Q47.6, R167.2
- new net N$133: D58.C, R179.2
- new net N$134: D57.C, R180.2
- new net N$135: C76.2, U21.1, Y7.P$2
- new net N$136: C77.1, U21.2, Y7.P$1
- new net N$137: D55.C, R175.2
- new net N$138: D56.C, R176.2
- new net N$139: JP26.1, R185.2
- new net N$140: JP27.1, R187.2
- new net N$141: D60.C, R188.2
- new net N$142: D61.C, R189.2
- new net N$143: D62.C, R190.2
- new net N$144: Q51.3, R188.1
- new net N$145: Q51.1, R191.1
- new net N$146: Q52.3, R180.1
- new net N$147: Q52.1, R192.1
- new net N$148: Q53.3, R189.1
- new net N$149: Q53.1, R193.1
- new net N$150: Q54.3, R190.1
- new net N$151: Q54.1, R194.1
- new net N$152: J31.SHLD1, J31.SHLD2, J31.SHLD3, J31.SHLD4, J31.SHLD5, J31.SHLD6, J31.SHLD7, J31.SHLD8, JP28.2
- new net N$153: Q55.3, Q56.1, R196.2
- new net N$154: Q55.2, Q55.5, Q55.6, R195.2
- new net N$155: D67.C, R207.2
- new net N$156: D66.C, R208.2
- new net N$157: C87.2, U24.1, Y8.P$2
- new net N$158: C88.1, U24.2, Y8.P$1
- new net N$159: D64.C, R203.2
- new net N$160: D65.C, R204.2
- new net N$161: JP30.1, R213.2
- new net N$162: JP31.1, R215.2
- new net N$163: D69.C, R216.2
- new net N$164: D70.C, R217.2
- new net N$165: D71.C, R218.2
- new net N$166: Q59.3, R216.1
- new net N$167: Q59.1, R219.1
- new net N$168: Q60.3, R208.1
- new net N$169: Q60.1, R220.1
- new net N$170: Q61.3, R217.1
- new net N$171: Q61.1, R221.1
- new net N$172: Q62.3, R218.1
- new net N$173: Q62.1, R222.1
- new net N$174: J36.SHLD1, J36.SHLD2, J36.SHLD3, J36.SHLD4, J36.SHLD5, J36.SHLD6, J36.SHLD7, J36.SHLD8, JP32.2
- new net N$175: Q63.3, Q64.1, R224.2
- new net N$176: Q63.2, Q63.5, Q63.6, R223.2
- new net N$177: D76.C, R235.2
- new net N$178: D75.C, R236.2
- new net N$179: C98.2, U27.1, Y9.P$2
- new net N$180: C99.1, U27.2, Y9.P$1
- new net N$181: D73.C, R231.2
- new net N$182: D74.C, R232.2
- new net N$183: JP34.1, R241.2
- new net N$184: JP35.1, R243.2
- new net N$185: D78.C, R244.2
- new net N$186: D79.C, R245.2
- new net N$187: D80.C, R246.2
- new net N$188: Q67.3, R244.1
- new net N$189: Q67.1, R247.1
- new net N$190: Q68.3, R236.1
- new net N$191: Q68.1, R248.1
- new net N$192: Q69.3, R245.1
- new net N$193: Q69.1, R249.1
- new net N$194: Q70.3, R246.1
- new net N$195: Q70.1, R250.1
- new net N$196: J41.SHLD1, J41.SHLD2, J41.SHLD3, J41.SHLD4, J41.SHLD5, J41.SHLD6, J41.SHLD7, J41.SHLD8, JP36.2
- new net N$197: Q71.3, Q72.1, R252.2
- new net N$198: Q71.2, Q71.5, Q71.6, R251.2
- new net N$199: D85.C, R263.2
- new net N$200: D84.C, R264.2
- new net N$201: C109.2, U30.1, Y10.P$2
- new net N$202: C110.1, U30.2, Y10.P$1
- new net N$203: D82.C, R259.2
- new net N$204: D83.C, R260.2
- new net N$205: JP38.1, R269.2
- new net N$206: JP39.1, R271.2
- new net N$207: D87.C, R272.2
- new net N$208: D88.C, R273.2
- new net N$209: D89.C, R274.2
- new net N$210: Q75.3, R272.1
- new net N$211: Q75.1, R275.1
- new net N$212: Q76.3, R264.1
- new net N$213: Q76.1, R276.1
- new net N$214: Q77.3, R273.1
- new net N$215: Q77.1, R277.1
- new net N$216: Q78.3, R274.1
- new net N$217: Q78.1, R278.1
- new net N$218: J46.SHLD1, J46.SHLD2, J46.SHLD3, J46.SHLD4, J46.SHLD5, J46.SHLD6, J46.SHLD7, J46.SHLD8, JP40.2
- new net N$219: Q79.3, Q80.1, R280.2
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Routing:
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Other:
- board text added: "v13"
- board text removed: "v12"

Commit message: Change to in stock 3.3V regulator
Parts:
- U1, U10, U13, U16, U19, U22, U25, U28, U3, U7: value AP2112K-3.3 -> 3.3V/150mA
